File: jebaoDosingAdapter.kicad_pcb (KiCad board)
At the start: 2 copper layers, 33.8 x 25.2 mm, 5 parts, among them J1 Conn_01x05_Male, J2 Conn_01x02_Male, J3 6P6C, U1 ULN2803A

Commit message: Add images and updated gerbers
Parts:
- removed the REF** at (105.0, 82.0)
- added G***: LOGO, ml_logo:ML_Logo, B.Cu at (99.3, 73.9)
- added H1: MountingHole, MountingHole:MountingHole_3.2mm_M3, F.Cu at (107.4, 59.4)
- added H2: MountingHole, MountingHole:MountingHole_3.2mm_M3, F.Cu at (107.4, 82.8)
- added H3: MountingHole, MountingHole:MountingHole_3.2mm_M3, F.Cu at (81.3, 59.4)
- added H4: MountingHole, MountingHole:MountingHole_3.2mm_M3, F.Cu at (81.3, 82.8)
- added REF**: OSHW-Logo2_9.8x8mm_SilkScreen, Symbol:OSHW-Logo2_9.8x8mm_SilkScreen, F.Cu at (94.2, 59.7)
- J1: footprint Connector_PinHeader_2.54mm:PinHeader_1x05_P2.54mm_Vertical -> Connector_JST:JST_XH_B05B-XH-A_1x05_P2.50mm_Vertical
- J2: footprint Connector_PinHeader_2.54mm:PinHeader_1x02_P2.54mm_Vertical -> Connector_JST:JST_XH_B02B-XH-A_1x02_P2.50mm_Vertical
- J3: moved to F.Cu
- U1: value ULN2803A -> ULN2803
- moved J3 10.9 mm to (87.6, 66.5)
- moved J1 1.09 mm to (106.9, 75.9), turned to 90 degrees
- moved J2 1.08 mm to (96.0, 83.1), turned to 180 degrees
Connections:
- J3 pad 2: Net-(J3-Pad2) -> /O2
- J3 pad 3: Net-(J3-Pad3) -> /O3
- J3 pad 4: Net-(J3-Pad4) -> /O1
- J3 pad 5: Net-(J3-Pad5) -> /O4
- U1 pad 15: Net-(J3-Pad4) -> /O4
- U1 pad 16: Net-(J3-Pad2) -> /O3
- U1 pad 17: Net-(J3-Pad3) -> /O2
- U1 pad 18: Net-(J3-Pad5) -> /O1
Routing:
- net Net-(J3-Pad4): track 19.7 -> 0.00 mm
- net /O1: track 0.00 -> 17.4 mm
- net Net-(J3-Pad2): track 14.3 -> 0.00 mm
- net /O2: track 0.00 -> 11.8 mm
- net Net-(J3-Pad3): track 8.72 -> 0.00 mm
- net Net-(J3-Pad5): track 8.46 -> 0.00 mm
- net /O4: track 0.00 -> 7.86 mm
- net /O3: track 0.00 -> 7.60 mm
- net +12V: track 43.0 -> 47.1 mm
- net Net-(J1-Pad4): track 7.21 -> 8.34 mm
- net Net-(J1-Pad3): track 6.20 -> 7.24 mm
- net Net-(J1-Pad2): track 5.67 -> 6.28 mm
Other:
- board size 33.8 x 25.2 mm -> 33.8 x 31 mm
- board text added: "+12v"
- board text added: "Jebao doser adapter github.com/ranthalion/ jebaoDosingAdapter"

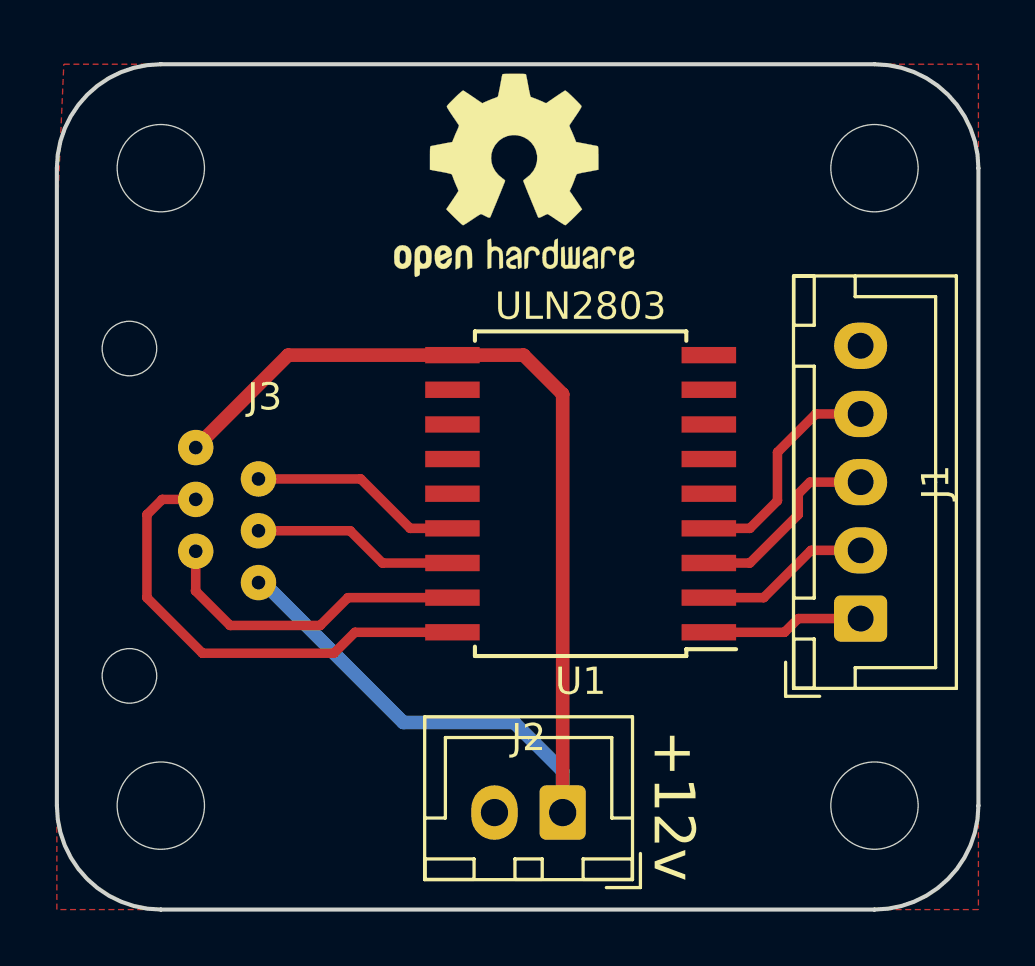
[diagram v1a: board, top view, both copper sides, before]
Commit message: Double up driver and document
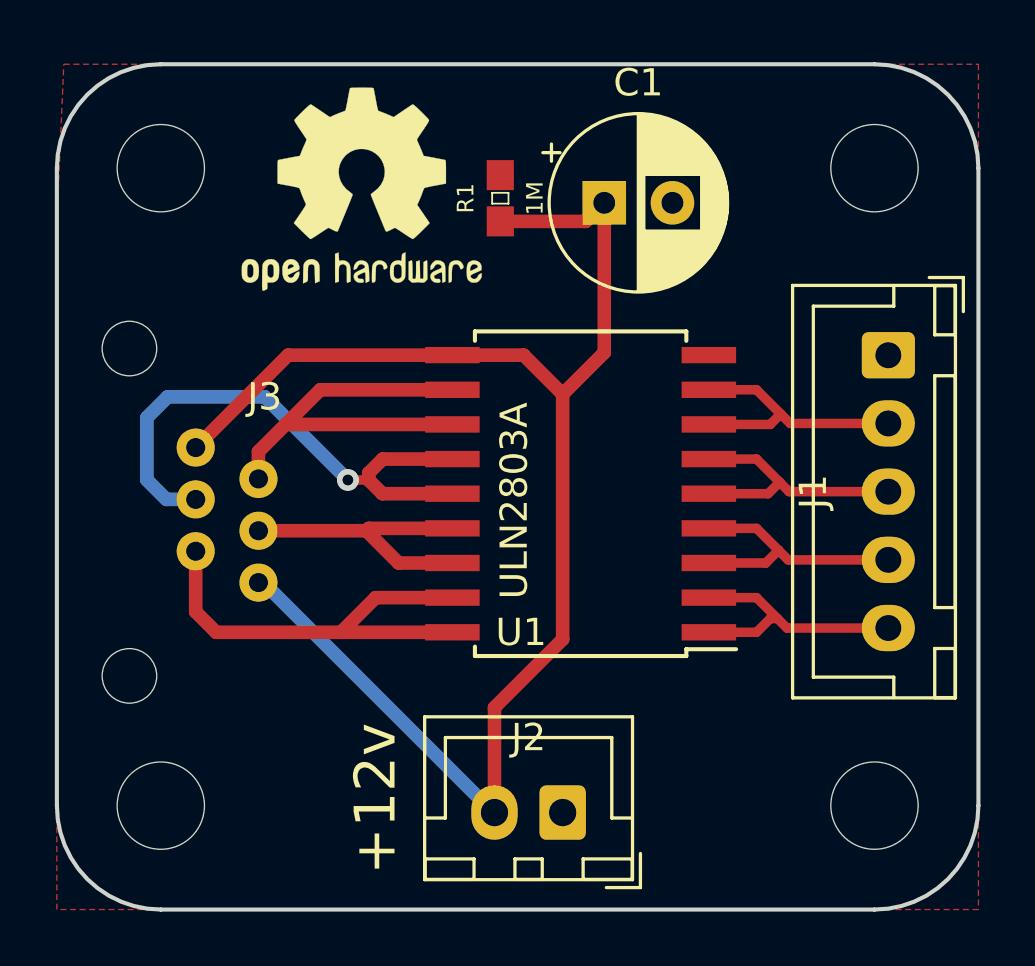
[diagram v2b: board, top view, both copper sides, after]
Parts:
- added C1: 47uF, Capacitor_THT:CP_Radial_D6.3mm_P2.50mm, F.Cu at (97.5, 60.7)
- added R1: 1M, Resistors:0603, F.Cu at (93.7, 60.5)
- J2: value Conn_01x02_Male -> Cp
- U1: value ULN2803 -> ULN2803A
- moved J1 9.71 mm to (108.0, 66.3), turned to 270 degrees
- moved REF** 5.61 mm to (88.6, 60.2)
- moved G*** 1.52 mm to (97.8, 73.9)
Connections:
- J1 pad 1: Net-(J1-Pad1) -> GND
- J1 pad 5: GND -> Net-(J1-Pad5)
- J2 pad 1: +12V -> GND
- J2 pad 2: GND -> +12V
- J3 pad 2: /O2 -> /P5
- J3 pad 3: /O3 -> /P6
- J3 pad 4: /O1 -> /P7
- J3 pad 5: /O4 -> /P8
- U1 pad 1: Net-(J1-Pad1) -> Net-(J1-Pad5)
- U1 pad 11: Net-(U1-Pad11) -> /P8
- U1 pad 12: Net-(U1-Pad12) -> /P8
- U1 pad 13: Net-(U1-Pad13) -> /P7
- U1 pad 14: Net-(U1-Pad14) -> /P7
- U1 pad 15: /O4 -> /P6
- U1 pad 16: /O3 -> /P6
- U1 pad 17: /O2 -> /P5
- U1 pad 18: /O1 -> /P5
- U1 pad 2: Net-(J1-Pad2) -> Net-(J1-Pad5)
- U1 pad 3: Net-(J1-Pad3) -> Net-(J1-Pad4)
- U1 pad 5: Net-(U1-Pad5) -> Net-(J1-Pad3)
- U1 pad 6: Net-(U1-Pad6) -> Net-(J1-Pad3)
- U1 pad 7: Net-(U1-Pad7) -> Net-(J1-Pad2)
- U1 pad 8: Net-(U1-Pad8) -> Net-(J1-Pad2)
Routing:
- net /P7: track 0.00 -> 20.9 mm, vias 0 -> 1
- net /O1: track 17.4 -> 0.00 mm
- net /P5: track 0.00 -> 16.6 mm
- net /P8: track 0.00 -> 15.2 mm
- net /O2: track 11.8 -> 0.00 mm
- net /P6: track 0.00 -> 10.8 mm
- net Net-(J1-Pad5): track 0.00 -> 9.77 mm
- net +12V: track 47.1 -> 56.5 mm
- net /O4: track 7.86 -> 0.00 mm
- net /O3: track 7.60 -> 0.00 mm
- net Net-(J1-Pad1): track 5.77 -> 0.00 mm
- net Net-(J1-Pad2): track 6.28 -> 9.89 mm
- net Net-(J1-Pad3): track 7.24 -> 9.85 mm
- net Net-(J1-Pad4): track 8.34 -> 9.81 mm
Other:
- board text added: "+"
- board text added: "GND"
- board text added: "P5"
- board text added: "P6"
- board text added: "P7"
- board text added: "P8"
